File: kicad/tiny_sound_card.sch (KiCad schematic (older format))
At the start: 48 parts, among them CON1 BARREL_JACK, IC1 ATMEGA328P-A, J1 TRS_JACK, M1 DFR0299, P1 EXT_PWR, P2 SPKOUT, P3 EXT_SW0, P4 EXT_I2C, P5 EXT_SW1, P6 EXT_I2C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

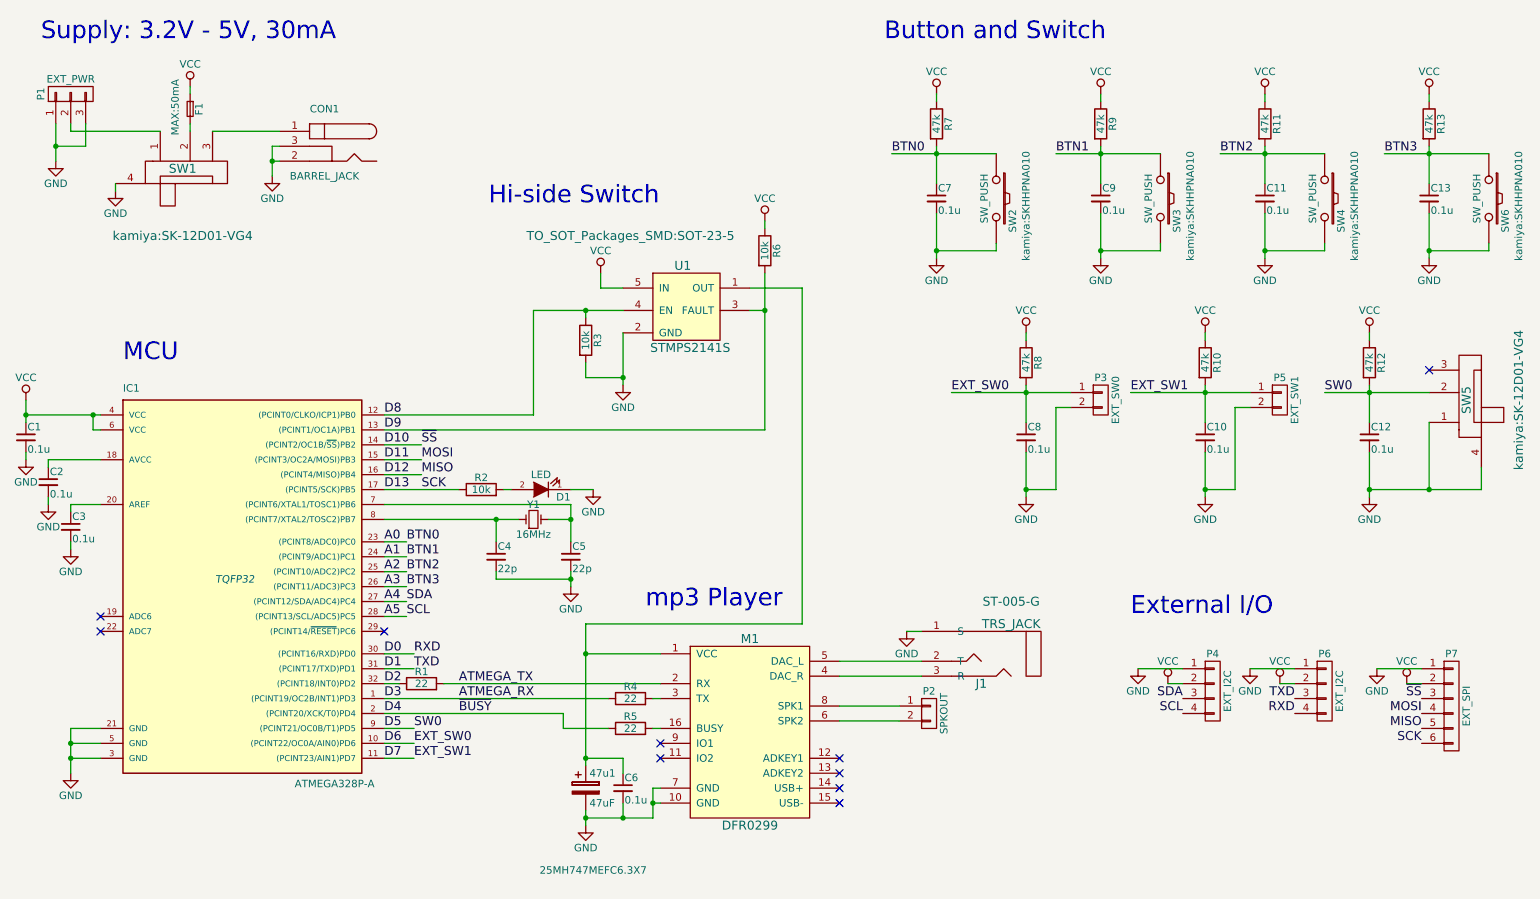
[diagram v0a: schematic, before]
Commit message: 部品割当の修正と、配置を完了
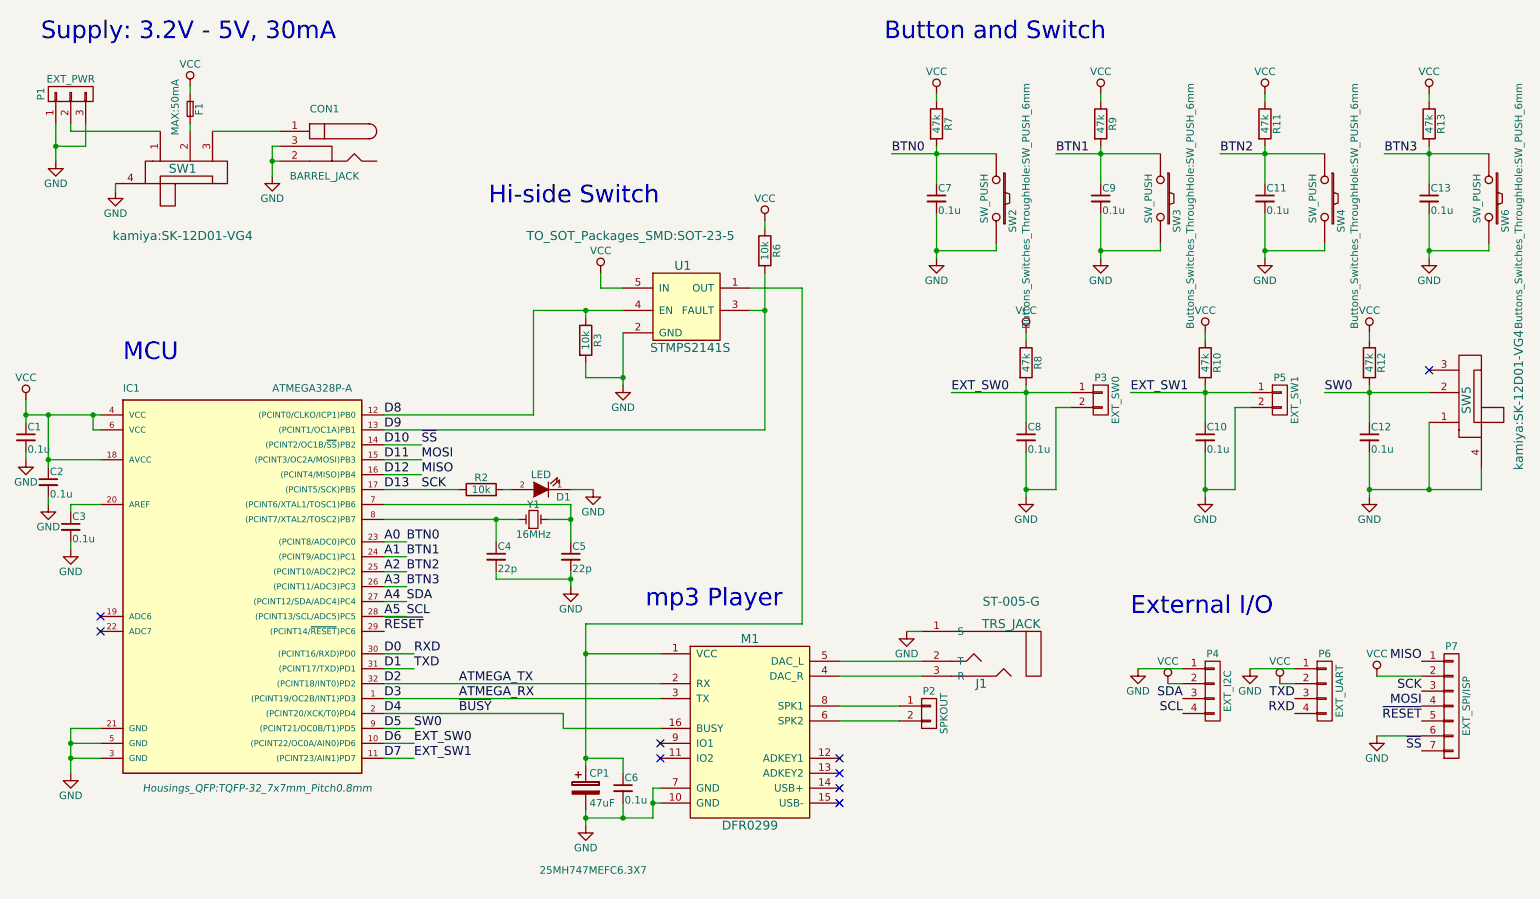
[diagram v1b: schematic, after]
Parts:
- removed P7: EXT_SPI, Pin_Headers:Pin_Header_Angled_1x06_Pitch2.54mm, symbol CONN_01X06
- removed R1, R4, R5: 22, Resistors_ThroughHole:R_Axial_DIN0207_L6.3mm_D2.5mm_P10.16mm_Horizontal, symbol R
- added P7: EXT_SPI/ISP, Pin_Headers:Pin_Header_Angled_1x07_Pitch2.54mm, symbol CONN_01X07
- IC1: footprint TQFP32 -> Housings_QFP:TQFP-32_7x7mm_Pitch0.8mm
- M1: footprint (none) -> kamiya:DFR0299
- P4: footprint (none) -> Pin_Headers:Pin_Header_Angled_1x04_Pitch2.54mm
- P6: value EXT_I2C -> EXT_UART; footprint (none) -> Pin_Headers:Pin_Header_Angled_1x04_Pitch2.54mm
- SW2, SW3, SW4, SW6: footprint kamiya:SKHHPNA010 -> Buttons_Switches_ThroughHole:SW_PUSH_6mm
- renumbered 47u1 to CP1
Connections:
- net D2 is gone; now on net ATMEGA_TX: IC1.32 ((PCINT18/INT0)PD2)
- net ATMEGA_RX: now also M1.3 (TX)
- net D10: now also P7.7 (P7)
- net D11: now also P7.4 (P4)
- net D12: now also P7.1 (P1)
- net D13: now also P7.3 (P3)
- net D4: now also M1.16 (BUSY)
- net GND: now also P7.6 (P6)
- net VCC: now also C2.1, IC1.18 (AVCC), P7.2 (P2)
- net ~RESET: now reaches IC1.29 ((PCINT14/~RESET~)PC6)
- net ~RESET: now also P7.5 (P5)
- no-connect marks 10 -> 9
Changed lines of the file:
@@
 P 2450 4700
 F 0 "IC1" H 1700 5950 50  0000 L BNN
-F 1 "ATMEGA328P-A" H 2850 3300 50  0000 L BNN
-F 2 "TQFP32" H 2450 4700 50  0000 C CIN
+F 1 "ATMEGA328P-A" H 2700 5950 50  0000 L BNN
+F 2 "Housings_QFP:TQFP-32_7x7mm_Pitch0.8mm" H 2600 3300 50  0000 C CIN
 F 3 "" H 2450 4700 50  0000 C CNN
 	1    2450 4700
@@
 F 0 "M1" H 5900 6300 60  0000 C CNN
 F 1 "DFR0299" H 5900 5050 60  0000 C CNN
-F 2 "" H 6000 5500 60  0000 C CNN
+F 2 "kamiya:DFR0299" H 6000 5500 60  0001 C CNN
 F 3 "" H 6000 5500 60  0000 C CNN
 	1    5900 5700
@@
 F 0 "SW2" H 7700 2260 50  0000 C CNN
 F 1 "SW_PUSH" H 7550 2070 50  0000 C CNN
-F 2 "kamiya:SKHHPNA010" H 7600 2350 50  0000 C CNN
+F 2 "Buttons_Switches_ThroughHole:SW_PUSH_6mm" H 7600 2350 50  0000 C CNN
 F 3 "" H 7550 2150 50  0000 C CNN
 	1    7550 2150
@@
 	1200 3900 1550 3900
 Wire Wire Line
-	1200 3900 1200 3950
+	1200 3600 1200 3950
 Wire Wire Line
 	1200 4150 1200 4200
@@
 Connection ~ 5250 6200
 $Comp
-L CP 47u1
+L CP CP1
 U 1 1 5B797C69
 P 4800 6100
-F 0 "47u1" H 4825 6200 50  0000 L CNN
+F 0 "CP1" H 4825 6200 50  0000 L CNN
 F 1 "47uF" H 4825 6000 50  0000 L CNN
 F 2 "Capacitors_ThroughHole:CP_Radial_D10.0mm_P2.50mm" H 4838 5950 50  0001 C CNN
@@
 Connection ~ 2700 1900
 $Comp
-L R R1
-U 1 1 5B79B972
-P 3700 5400
-F 0 "R1" V 3780 5400 50  0000 C CNN
-F 1 "22" V 3700 5400 50  0000 C CNN
-F 2 "Resistors_ThroughHole:R_Axial_DIN0207_L6.3mm_D2.5mm_P10.16mm_Horizontal" V 3630 5400 50  0001 C CNN
-F 3 "" H 3700 5400 50  0000 C CNN
-	1    3700 5400
-	0    -1   -1   0
-$EndComp
-$Comp
 L R R2
 U 1 1 5B79BCA9
@@
 	0    -1   -1   0
 $EndComp
-$Comp
-L R R4
-U 1 1 5B79C32F
-P 5100 5500
-F 0 "R4" V 5180 5500 50  0000 C CNN
-F 1 "22" V 5100 5500 50  0000 C CNN
-F 2 "Resistors_ThroughHole:R_Axial_DIN0207_L6.3mm_D2.5mm_P10.16mm_Horizontal" V 5030 5500 50  0001 C CNN
-F 3 "" H 5100 5500 50  0000 C CNN
-	1    5100 5500
-	0    -1   -1   0
-$EndComp
 Wire Wire Line
 	4800 5900 5050 5900
@@
 Connection ~ 4800 5900
 Wire Wire Line
-	5300 5500 5250 5500
-Wire Wire Line
-	5300 5400 3850 5400
-Wire Wire Line
-	3550 5400 3450 5400
-Wire Wire Line
-	3450 5500 4950 5500
-$Comp
-L R R5
-U 1 1 5B79CFB9
-P 5100 5700
-F 0 "R5" V 5180 5700 50  0000 C CNN
-F 1 "22" V 5100 5700 50  0000 C CNN
-F 2 "Resistors_ThroughHole:R_Axial_DIN0207_L6.3mm_D2.5mm_P10.16mm_Horizontal" V 5030 5700 50  0001 C CNN
-F 3 "" H 5100 5700 50  0000 C CNN
-	1    5100 5700
-	0    -1   -1   0
-$EndComp
-Wire Wire Line
-	5250 5700 5300 5700
-Wire Wire Line
-	4950 5700 4650 5700
+	3450 5500 5300 5500
+Wire Wire Line
+	3450 5400 5300 5400
+Wire Wire Line
+	4650 5700 5300 5700
 Wire Wire Line
 	4650 5600 3450 5600
@@
 F 0 "SW3" H 8800 2260 50  0000 C CNN
 F 1 "SW_PUSH" H 8650 2070 50  0000 C CNN
-F 2 "kamiya:SKHHPNA010" H 8700 2350 50  0000 C CNN
+F 2 "Buttons_Switches_ThroughHole:SW_PUSH_6mm" H 8700 2350 50  0000 C CNN
 F 3 "" H 8650 2150 50  0000 C CNN
 	1    8650 2150
@@
 F 0 "SW4" H 9900 2260 50  0000 C CNN
 F 1 "SW_PUSH" H 9750 2070 50  0000 C CNN
-F 2 "kamiya:SKHHPNA010" H 9800 2350 50  0000 C CNN
+F 2 "Buttons_Switches_ThroughHole:SW_PUSH_6mm" H 9800 2350 50  0000 C CNN
 F 3 "" H 9750 2150 50  0000 C CNN
 	1    9750 2150
@@
 F 0 "SW6" H 11000 2260 50  0000 C CNN
 F 1 "SW_PUSH" H 10850 2070 50  0000 C CNN
-F 2 "kamiya:SKHHPNA010" H 10900 2350 50  0000 C CNN
+F 2 "Buttons_Switches_ThroughHole:SW_PUSH_6mm" H 10900 2350 50  0000 C CNN
 F 3 "" H 10850 2150 50  0000 C CNN
 	1    10850 2150
@@
 NoConn ~ 1550 4950
 NoConn ~ 1550 5050
-Text Label 10400 5800 2    60   ~ 0
+Text Label 10400 5450 2    60   ~ 0
 SCK
-Text Label 10400 5700 2    60   ~ 0
+Text Label 10400 5250 2    60   ~ 0
 MISO
-Text Label 10400 5600 2    60   ~ 0
+Text Label 10400 5550 2    60   ~ 0
 MOSI
-Text Label 10400 5500 2    60   ~ 0
+Text Label 10400 5850 2    60   ~ 0
 ~SS
 $Comp
@@
 F 0 "P4" H 9000 5700 50  0000 C CNN
 F 1 "EXT_I2C" V 9100 5450 50  0000 C CNN
-F 2 "" H 9000 5450 50  0000 C CNN
+F 2 "Pin_Headers:Pin_Header_Angled_1x04_Pitch2.54mm" H 9000 5450 50  0001 C CNN
 F 3 "" H 9000 5450 50  0000 C CNN
 	1    9000 5450
@@
 P 9750 5450
 F 0 "P6" H 9750 5700 50  0000 C CNN
-F 1 "EXT_I2C" V 9850 5450 50  0000 C CNN
-F 2 "" H 9750 5450 50  0000 C CNN
+F 1 "EXT_UART" V 9850 5450 50  0000 C CNN
+F 2 "Pin_Headers:Pin_Header_Angled_1x04_Pitch2.54mm" H 9750 5450 50  0001 C CNN
 F 3 "" H 9750 5450 50  0000 C CNN
 	1    9750 5450
@@
 	9450 5400 9550 5400
 $Comp
-L CONN_01X06 P7
-U 1 1 5B7AAA58
+L VCC #PWR035
+U 1 1 5B7AAB9D
+P 10100 5350
+F 0 "#PWR035" H 10100 5200 50  0001 C CNN
+F 1 "VCC" H 10100 5500 50  0000 C CNN
+F 2 "" H 10100 5350 50  0000 C CNN
+F 3 "" H 10100 5350 50  0000 C CNN
+	1    10100 5350
+	1    0    0    -1
+$EndComp
+$Comp
+L CONN_01X07 P7
+U 1 1 5B7B56B1
 P 10600 5550
-F 0 "P7" H 10600 5900 50  0000 C CNN
-F 1 "EXT_SPI" V 10700 5550 50  0000 C CNN
-F 2 "Pin_Headers:Pin_Header_Angled_1x06_Pitch2.54mm" H 10600 5550 50  0001 C CNN
+F 0 "P7" H 10600 5950 50  0000 C CNN
+F 1 "EXT_SPI/ISP" V 10700 5550 50  0000 C CNN
+F 2 "Pin_Headers:Pin_Header_Angled_1x07_Pitch2.54mm" H 10600 5550 50  0001 C CNN
 F 3 "" H 10600 5550 50  0000 C CNN
 	1    10600 5550
 	1    0    0    -1
 $EndComp
-$Comp
-L GND #PWR035
-U 1 1 5B7AAB97
-P 10100 5300
-F 0 "#PWR035" H 10100 5050 50  0001 C CNN
-F 1 "GND" H 10100 5150 50  0000 C CNN
-F 2 "" H 10100 5300 50  0000 C CNN
-F 3 "" H 10100 5300 50  0000 C CNN
-	1    10100 5300
-	1    0    0    -1
-$EndComp
-$Comp
-L VCC #PWR036
-U 1 1 5B7AAB9D
-P 10300 5400
-F 0 "#PWR036" H 10300 5250 50  0001 C CNN
-F 1 "VCC" H 10300 5550 50  0000 C CNN
-F 2 "" H 10300 5400 50  0000 C CNN
-F 3 "" H 10300 5400 50  0000 C CNN
-	1    10300 5400
-	1    0    0    -1
-$EndComp
-Wire Wire Line
-	10100 5300 10400 5300
-Wire Wire Line
-	10300 5400 10400 5400
-NoConn ~ 3450 5050
+Wire Wire Line
+	10100 5350 10400 5350
+Text Label 3450 5050 0    60   ~ 0
+~RESET
+Text Label 10400 5650 2    60   ~ 0
+~RESET
+$Comp
+L GND #PWR036
+U 1 1 5B7B7DEC
+P 10100 5750
+F 0 "#PWR036" H 10100 5500 50  0001 C CNN
+F 1 "GND" H 10100 5600 50  0000 C CNN
+F 2 "" H 10100 5750 50  0000 C CNN
+F 3 "" H 10100 5750 50  0000 C CNN
+	1    10100 5750
+	1    0    0    -1
+$EndComp
+Wire Wire Line
+	10100 5750 10400 5750
+Connection ~ 1200 3600
+Connection ~ 1200 3900
 $EndSCHEMATC

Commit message: GPIOのアサインを大幅に調整
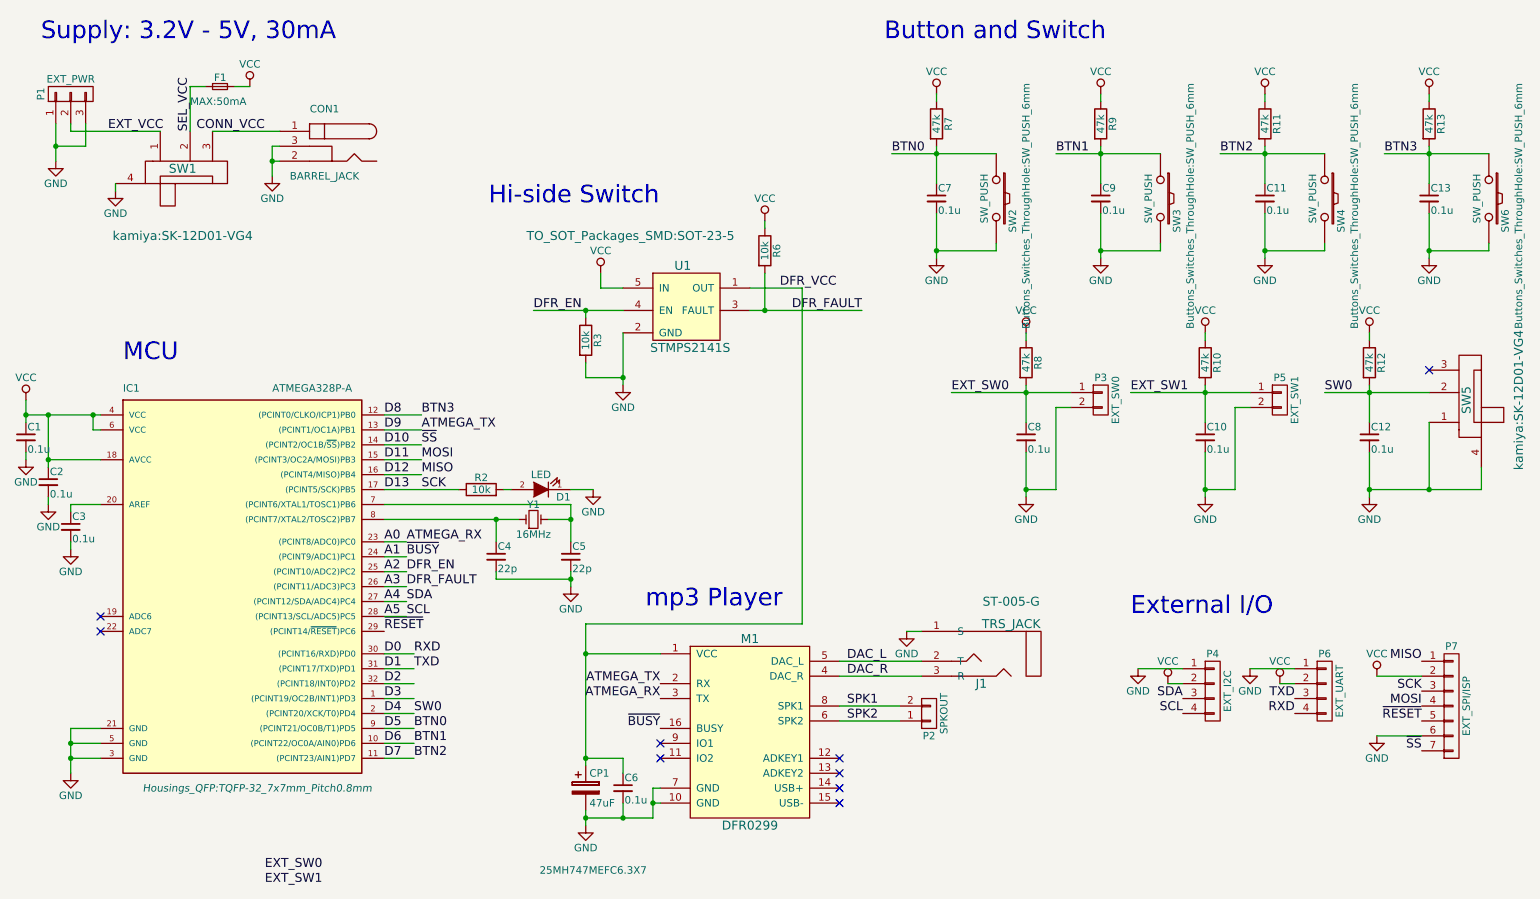
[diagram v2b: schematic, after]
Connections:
- net A0: now also M1.3 (TX); no longer C7.1, R7.2, SW2.1
- net A1: now also M1.16 (BUSY); no longer C9.1, R9.2, SW3.1
- net A2: now also R3.1, U1.4 (EN); no longer C11.1, R11.2, SW4.1
- net A3: now also R6.2, U1.3 (FAULT); no longer C13.1, R13.2, SW6.1
- net ATMEGA_TX: now also IC1.13 ((PCINT1/OC1A)PB1); no longer IC1.32 ((PCINT18/INT0)PD2)
- net D4: now also C12.1, R12.2, SW5.2; no longer M1.16 (BUSY)
- net VCC: now also F1.2; no longer F1.1
- net DFR_VCC: now reaches C6.1, CP1.1, M1.1 (VCC), U1.1 (OUT)
- net DAC_R: now reaches J1.3 (R), M1.4 (DAC_R)
- net DAC_L: now reaches J1.2 (T), M1.5 (DAC_L)
- net SPK1: now reaches P2.2 (P2)
- net SPK1: now also M1.8 (SPK1); no longer M1.6 (SPK2)
- net SPK2: now reaches P2.1 (P1)
- net SPK2: now also M1.6 (SPK2); no longer M1.8 (SPK1)
- net EXT_VCC: now reaches P1.2 (P2), SW1.1
- net SEL_VCC: now reaches SW1.2
- net SEL_VCC: now also F1.1; no longer F1.2
- net CONN_VCC: now reaches CON1.1, SW1.3
- net ATMEGA_RX renamed D3
- net D3: no longer M1.3 (TX)
- removed net D5: C12.1, IC1.9 ((PCINT21/OC0B/T1)PD5), R12.2, SW5.2
- net D6 renamed EXT_SW0
- net EXT_SW0: no longer IC1.10 ((PCINT22/OC0A/AIN0)PD6)
- net D7 renamed EXT_SW1
- net EXT_SW1: no longer IC1.11 ((PCINT23/AIN1)PD7)
- removed net D8: IC1.12 ((PCINT0/CLKO/ICP1)PB0), R3.1, U1.4 (EN)
- removed net D9: IC1.13 ((PCINT1/OC1A)PB1), R6.2, U1.3 (FAULT)
- new net BTN0: C7.1, IC1.9 ((PCINT21/OC0B/T1)PD5), R7.2, SW2.1
- new net BTN1: C9.1, IC1.10 ((PCINT22/OC0A/AIN0)PD6), R9.2, SW3.1
- new net BTN2: C11.1, IC1.11 ((PCINT23/AIN1)PD7), R11.2, SW4.1
- new net BTN3: C13.1, IC1.12 ((PCINT0/CLKO/ICP1)PB0), R13.2, SW6.1
- new net D2: IC1.32 ((PCINT18/INT0)PD2)
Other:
- moved on the sheet: F1
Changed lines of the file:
@@
 L VCC #PWR04
 U 1 1 5B793B69
-P 2150 1400
-F 0 "#PWR04" H 2150 1250 50  0001 C CNN
-F 1 "VCC" H 2150 1550 50  0000 C CNN
-F 2 "" H 2150 1400 50  0000 C CNN
-F 3 "" H 2150 1400 50  0000 C CNN
-	1    2150 1400
-	1    0    0    -1
-$EndComp
-Wire Wire Line
-	2150 1650 2150 1700
+P 2550 1400
+F 0 "#PWR04" H 2550 1250 50  0001 C CNN
+F 1 "VCC" H 2550 1550 50  0000 C CNN
+F 2 "" H 2550 1400 50  0000 C CNN
+F 3 "" H 2550 1400 50  0000 C CNN
+	1    2550 1400
+	1    0    0    -1
+$EndComp
+Wire Wire Line
+	2150 1400 2150 1700
 $Comp
 L CONN_01X03 P1
@@
 L F_Small F1
 U 1 1 5B79423D
-P 2150 1550
-F 0 "F1" H 2110 1610 50  0000 L CNN
-F 1 "MAX:50mA" H 1950 1450 50  0000 L CNN
-F 2 "Capacitors_ThroughHole:C_Rect_L7.0mm_W4.5mm_P5.00mm" H 2150 1550 50  0001 C CNN
-F 3 "" H 2150 1550 50  0000 C CNN
-	1    2150 1550
-	0    1    1    0
-$EndComp
-Wire Wire Line
-	2150 1400 2150 1450
+P 2350 1400
+F 0 "F1" H 2310 1460 50  0000 L CNN
+F 1 "MAX:50mA" H 2150 1300 50  0000 L CNN
+F 2 "Capacitors_ThroughHole:C_Rect_L7.0mm_W4.5mm_P5.00mm" H 2350 1400 50  0001 C CNN
+F 3 "" H 2350 1400 50  0000 C CNN
+	1    2350 1400
+	1    0    0    -1
+$EndComp
+Wire Wire Line
+	2550 1400 2450 1400
 $Comp
 L VCC #PWR06
@@
 Wire Wire Line
 	4250 4100 4300 4100
-Text Label 3950 5400 0    60   ~ 0
+Text Label 3700 3700 0    60   ~ 0
 ATMEGA_TX
-Text Label 3950 5500 0    60   ~ 0
+Text Label 3600 4450 0    60   ~ 0
 ATMEGA_RX
 $Comp
@@
 NoConn ~ 6500 6100
 NoConn ~ 6500 6200
-Wire Wire Line
-	4650 5700 4650 5600
-Text Label 3950 5600 0    60   ~ 0
+Text Label 3600 4550 0    60   ~ 0
 ~BUSY
 $Comp
@@
 F 3 "" H 7100 5600 50  0000 C CNN
 	1    7100 5600
-	1    0    0    -1
+	1    0    0    1
 $EndComp
 Wire Wire Line
@@
 	5050 5900 5050 6000
 Connection ~ 4800 5900
-Wire Wire Line
-	3450 5500 5300 5500
-Wire Wire Line
-	3450 5400 5300 5400
-Wire Wire Line
-	4650 5700 5300 5700
-Wire Wire Line
-	4650 5600 3450 5600
 $Comp
 L TRS_JACK J1
@@
 Text Label 10150 1850 0    60   ~ 0
 BTN3
-Text Label 3600 4450 0    60   ~ 0
+Text Label 3650 5700 0    60   ~ 0
 BTN0
-Text Label 3600 4550 0    60   ~ 0
+Text Label 3650 5800 0    60   ~ 0
 BTN1
-Text Label 3600 4650 0    60   ~ 0
+Text Label 3650 5900 0    60   ~ 0
 BTN2
-Text Label 3600 4750 0    60   ~ 0
+Text Label 3700 3600 0    60   ~ 0
 BTN3
 Wire Wire Line
@@
 Text Label 8800 5600 2    60   ~ 0
 SCL
-Text Label 3650 5700 0    60   ~ 0
+Text Label 3650 5600 0    60   ~ 0
 SW0
 Wire Wire Line
@@
 Wire Wire Line
 	4800 2900 4800 2950
-Wire Wire Line
-	4450 2900 4450 3600
-Wire Wire Line
-	4450 3600 3450 3600
 Connection ~ 4800 2900
 $Comp
@@
 Connection ~ 4800 5200
 Wire Wire Line
-	5900 2900 6000 2900
-Wire Wire Line
-	6000 2650 6000 3700
+	5900 2900 6650 2900
 $Comp
 L VCC #PWR026
@@
 Wire Wire Line
 	6000 2300 6000 2350
-Wire Wire Line
-	6000 3700 3450 3700
 Connection ~ 6000 2900
 Wire Wire Line
@@
 Text Notes 5200 4900 0    118  ~ 0
 mp3 Player
-Text Label 3650 5800 0    60   ~ 0
+Text Label 2650 6650 0    60   ~ 0
 EXT_SW0
-Text Label 3650 5900 0    60   ~ 0
+Text Label 2650 6750 0    60   ~ 0
 EXT_SW1
 Text Label 8450 3450 0    60   ~ 0
@@
 Connection ~ 1200 3600
 Connection ~ 1200 3900
+Wire Wire Line
+	2250 1400 2150 1400
+Text Label 1600 1700 0    60   ~ 0
+EXT_VCC
+Text Label 2650 1700 2    60   ~ 0
+CONN_VCC
+Text Label 2150 1700 1    60   ~ 0
+SEL_VCC
+Text Label 6100 2750 0    60   ~ 0
+DFR_VCC
+Text Label 6550 5250 0    60   ~ 0
+DAC_L
+Text Label 6550 5350 0    60   ~ 0
+DAC_R
+Text Label 6550 5550 0    60   ~ 0
+SPK1
+Text Label 6550 5650 0    60   ~ 0
+SPK2
+Wire Wire Line
+	3450 3600 3700 3600
+Wire Wire Line
+	3450 3700 3700 3700
+Wire Wire Line
+	6000 2900 6000 2650
+Text Label 4450 2900 0    60   ~ 0
+DFR_EN
+Text Label 6650 2900 2    60   ~ 0
+DFR_FAULT
+Text Label 3600 4650 0    60   ~ 0
+DFR_EN
+Wire Wire Line
+	3450 5400 3650 5400
+Wire Wire Line
+	3450 5500 3650 5500
+Wire Wire Line
+	3450 5600 3650 5600
+Text Label 5300 5400 2    60   ~ 0
+ATMEGA_TX
+Text Label 5300 5500 2    60   ~ 0
+ATMEGA_RX
+Text Label 5300 5700 2    60   ~ 0
+~BUSY
+Text Label 3600 4750 0    60   ~ 0
+DFR_FAULT
 $EndSCHEMATC
